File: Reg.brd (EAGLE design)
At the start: 15.2 x 21 mm, 12 parts, among them Q1 NPN2SC3422-2, Q2 NPN2SC3325, Q3 PNP2SA1313

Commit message: 完成
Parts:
- D1: value RED -> SHORT
- D2: value BLUE -> SHORT
- D3, D4: value (none) -> BLUE
- R1, R4: value 1k -> 1.5k
- R2: value DNP -> 1.5k
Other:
- board text added: "LED REG ver2"
- board text removed: "REG ver1"
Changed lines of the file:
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@@
 <setting verticaltext="up"/>
 </settings>
-<grid distance="12.5" unitdist="mil" unit="mil" style="lines" multiple="4" display="yes" altdistance="5" altunitdist="mil" altunit="mil"/>
+<grid distance="25" unitdist="mil" unit="mil" style="lines" multiple="4" display="yes" altdistance="5" altunitdist="mil" altunit="mil"/>
 <layers>
 <layer number="1" name="Top" color="4" fill="1" visible="yes" active="yes"/>
@@
 <board>
 <plain>
-<text x="3.81" y="18.0975" size="1.27" layer="21">REG ver1</text>
+<text x="14.2875" y="1.905" size="1.27" layer="21" rot="R90">LED REG ver2</text>
 <wire x1="0" y1="0" x2="15.24" y2="0" width="0.2032" layer="20"/>
 <wire x1="15.24" y1="0" x2="15.24" y2="20.955" width="0.2032" layer="20"/>
@@
 </autorouter>
 <elements>
-<element name="D1" library="my_rcl" package="D1608" value="RED" x="2.54" y="8.255" smashed="yes" rot="MR90">
+<element name="D1" library="my_rcl" package="D1608" value="SHORT" x="2.54" y="8.255" smashed="yes" rot="MR90">
 <attribute name="NAME" x="3.5075" y="7.455" size="0.8128" layer="26" rot="MR90"/>
 <attribute name="VALUE" x="0.89" y="7.455" size="0.8128" layer="28" rot="MR90"/>
 </element>
-<element name="D2" library="my_rcl" package="D1608" value="BLUE" x="2.54" y="4.7625" smashed="yes" rot="MR90">
-<attribute name="NAME" x="3.19" y="3.9625" size="0.8128" layer="26" rot="MR90"/>
+<element name="D2" library="my_rcl" package="D1608" value="SHORT" x="2.54" y="4.7625" smashed="yes" rot="MR90">
+<attribute name="NAME" x="3.825" y="3.9625" size="0.8128" layer="26" rot="MR90"/>
 <attribute name="VALUE" x="0.89" y="3.9625" size="0.8128" layer="28" rot="MR90"/>
 </element>
 <element name="JP1" library="pinhead" library_urn="urn:adsk.eagle:library:325" package="1X03" package3d_urn="urn:adsk.eagle:package:22458/2" value="CON" x="7.62" y="2.54" smashed="yes">
 <attribute name="POPULARITY" value="92" x="25.4" y="-1.27" size="1.778" layer="27" display="off"/>
-<attribute name="VALUE" x="3.81" y="-0.635" size="1.27" layer="27"/>
 </element>
 <element name="Q1" library="my_ic" package="TO126-2" value="NPN2SC3422-2" x="7.62" y="6.6675" smashed="yes">
-<attribute name="NAME" x="9.525" y="4.445" size="0.8128" layer="25"/>
+<attribute name="NAME" x="13.335" y="15.24" size="0.8128" layer="25" rot="R90"/>
 <attribute name="VALUE" x="3.81" y="9.8425" size="0.8128" layer="27"/>
 </element>
 <element name="Q2" library="my_ic" package="SC59" value="NPN2SC3325" x="9.2075" y="10.16" smashed="yes" rot="MR180">
-<attribute name="NAME" x="7.3025" y="10.795" size="0.8128" layer="26" rot="MR270"/>
+<attribute name="NAME" x="10.16" y="13.0175" size="0.8128" layer="26" rot="MR180"/>
 <attribute name="VALUE" x="7.3025" y="13.335" size="0.8128" layer="28" rot="MR180"/>
 </element>
-<element name="R2" library="my_rcl" package="1608" value="DNP" x="12.7" y="4.7625" smashed="yes" rot="MR90">
-<attribute name="NAME" x="12.395" y="8.3025" size="0.8128" layer="26" rot="MR0"/>
+<element name="R2" library="my_rcl" package="1608" value="1.5k" x="12.7" y="4.7625" smashed="yes" rot="MR90">
+<attribute name="NAME" x="14.5575" y="5.41" size="0.8128" layer="26" rot="MR270"/>
 <attribute name="VALUE" x="10.9" y="3.1625" size="0.8128" layer="28" rot="MR90"/>
 </element>
 <element name="Q3" library="my_ic" package="SC59" value="PNP2SA1313" x="5.08" y="10.16" smashed="yes" rot="MR180">
-<attribute name="NAME" x="4.445" y="7.9375" size="0.8128" layer="26" rot="MR180"/>
+<attribute name="NAME" x="3.4925" y="12.7" size="0.8128" layer="26" rot="MR270"/>
 <attribute name="VALUE" x="3.175" y="13.335" size="0.8128" layer="28" rot="MR180"/>
 </element>
-<element name="R1" library="my_rcl" package="1608" value="1k" x="2.54" y="10.795" smashed="yes" rot="R270">
-<attribute name="NAME" x="3.54" y="12.395" size="0.8128" layer="25" rot="R270"/>
+<element name="R1" library="my_rcl" package="1608" value="1.5k" x="2.54" y="10.795" smashed="yes" rot="R270">
+<attribute name="NAME" x="1.575" y="10.525" size="0.8128" layer="25" rot="R90"/>
 <attribute name="VALUE" x="0.74" y="12.395" size="0.8128" layer="27" rot="R270"/>
 </element>
-<element name="R4" library="my_rcl" package="1608" value="1k" x="2.54" y="7.62" smashed="yes" rot="R90">
-<attribute name="NAME" x="1.6" y="6.3025" size="0.8128" layer="25" rot="R180"/>
+<element name="R4" library="my_rcl" package="1608" value="1.5k" x="2.54" y="7.62" smashed="yes" rot="R90">
+<attribute name="NAME" x="0.6825" y="8.585" size="0.8128" layer="25" rot="R270"/>
 <attribute name="VALUE" x="4.34" y="6.02" size="0.8128" layer="27" rot="R90"/>
 </element>
 <element name="C7" library="my_rcl" package="1608" value="100p" x="7.3025" y="13.335" smashed="yes" rot="MR180">
-<attribute name="NAME" x="5.7025" y="12.335" size="0.8128" layer="26" rot="MR180"/>
+<attribute name="NAME" x="4.81" y="12.6875" size="0.8128" layer="26" rot="MR90"/>
 <attribute name="VALUE" x="5.7025" y="15.135" size="0.8128" layer="28" rot="MR180"/>
 </element>
-<element name="D3" library="my_rcl" package="D1608" value="" x="12.7" y="8.255" smashed="yes" rot="MR90">
+<element name="D3" library="my_rcl" package="D1608" value="BLUE" x="12.7" y="8.255" smashed="yes" rot="MR90">
 <attribute name="NAME" x="13.6675" y="7.455" size="0.8128" layer="26" rot="MR90"/>
 <attribute name="VALUE" x="11.05" y="7.455" size="0.8128" layer="28" rot="MR90"/>
 </element>
-<element name="D4" library="my_rcl" package="D1608" value="" x="12.7" y="11.43" smashed="yes" rot="MR90">
+<element name="D4" library="my_rcl" package="D1608" value="BLUE" x="12.7" y="11.43" smashed="yes" rot="MR90">
 <attribute name="NAME" x="13.6675" y="10.63" size="0.8128" layer="26" rot="MR90"/>
 <attribute name="VALUE" x="11.05" y="10.63" size="0.8128" layer="28" rot="MR90"/>

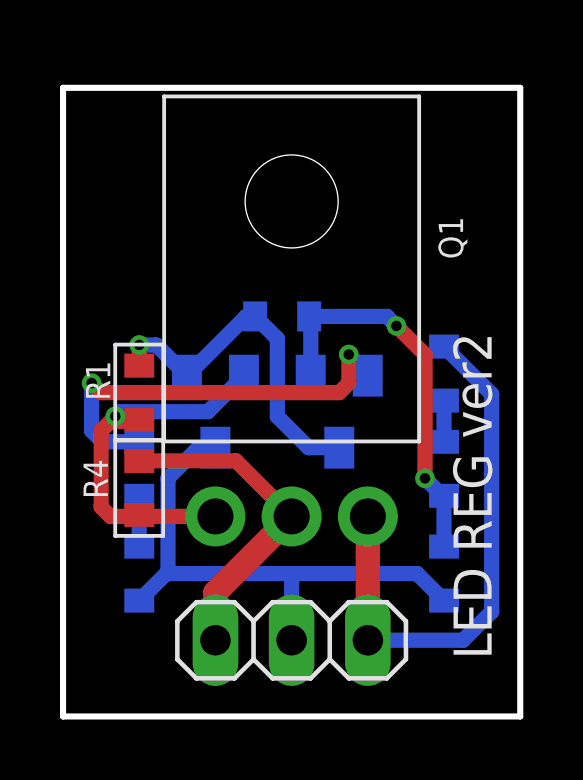
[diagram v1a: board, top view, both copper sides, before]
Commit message: 帰還ループの改善
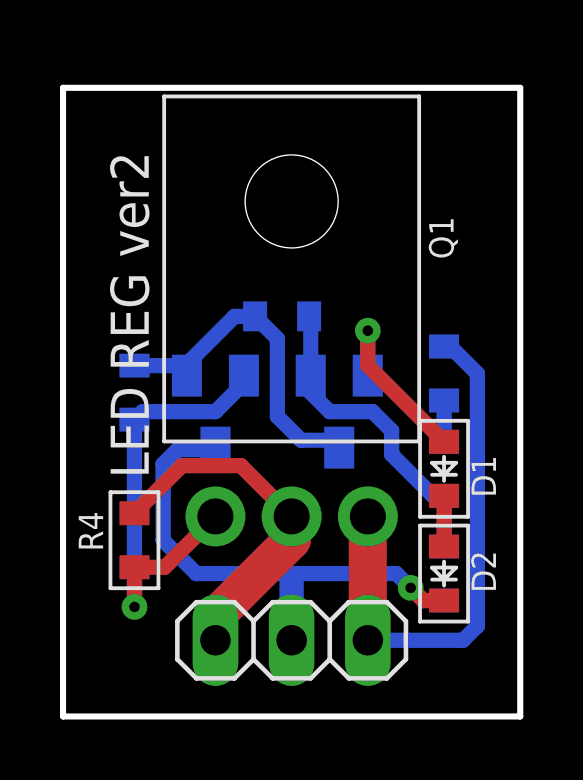
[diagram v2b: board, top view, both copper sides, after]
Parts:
- moved D1 10.2 mm to (12.7, 8.26), flipped to the top
- moved D2 10.2 mm to (12.7, 4.76), flipped to the top
- moved R4 1.75 mm to (2.38, 5.87)
- moved R1 0.16 mm to (2.38, 10.8), flipped to the bottom
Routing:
- net N$4: track 14.1 -> 6.26 mm, vias 2 -> 1
- net N$3: track 13.1 -> 10.6 mm, vias 2 -> 0
- net N$1: track 13.0 -> 15.4 mm
- net IN: track 11.0 -> 11.8 mm
- net N$10: track 11.9 -> 11.3 mm, vias 1 -> 0
- net GND: track 18.3 -> 18.2 mm, vias 0 -> 1

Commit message: チップオンリーも
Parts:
- added Q4: NPN2SC3325, my_ic:SC59
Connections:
- net IN: now also Q4.3
- net N$1: now also Q4.1
- net OUT: now also Q4.2
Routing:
- net OUT: track 17.9 -> 24.3 mm
- net N$1: track 15.4 -> 19.6 mm, vias 1 -> 2
- net IN: track 11.8 -> 14.2 mm
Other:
- board size 15.2 x 21 mm -> 25.4 x 21 mm
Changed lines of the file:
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@@
 <setting verticaltext="up"/>
 </settings>
-<grid distance="6.25" unitdist="mil" unit="mil" style="lines" multiple="4" display="yes" altdistance="5" altunitdist="mil" altunit="mil"/>
+<grid distance="12.5" unitdist="mil" unit="mil" style="lines" multiple="4" display="yes" altdistance="5" altunitdist="mil" altunit="mil"/>
 <layers>
 <layer number="1" name="Top" color="4" fill="1" visible="yes" active="yes"/>
@@
 <wire x1="15.24" y1="20.955" x2="0" y2="20.955" width="0.2032" layer="20"/>
 <wire x1="0" y1="20.955" x2="0" y2="0" width="0.2032" layer="20"/>
+<wire x1="15.24" y1="20.955" x2="25.4" y2="20.955" width="0.2032" layer="20"/>
+<wire x1="25.4" y1="20.955" x2="25.4" y2="0" width="0.2032" layer="20"/>
+<wire x1="25.4" y1="0" x2="15.24" y2="0" width="0.2032" layer="20"/>
 </plain>
 <attributes>
@@
 <attribute name="VALUE" x="11.05" y="10.63" size="0.8128" layer="28" rot="MR90"/>
 </element>
+<element name="Q4" library="my_ic" package="SC59" value="NPN2SC3325" x="6.35" y="10.795" smashed="yes" rot="R90">
+<attribute name="NAME" x="4.1275" y="8.89" size="0.8128" layer="25" rot="R90"/>
+<attribute name="VALUE" x="9.525" y="8.89" size="0.8128" layer="27" rot="R90"/>
+</element>
 </elements>
 <signals>
@@
 <wire x1="13.335" y1="2.54" x2="10.16" y2="2.54" width="0.508" layer="16"/>
 <wire x1="13.81125" y1="11.43" x2="13.81125" y2="3.01625" width="0.508" layer="16"/>
+<contactref element="Q4" pad="2"/>
+<wire x1="7.55" y1="11.745" x2="7.94" y2="11.745" width="0.8128" layer="1"/>
+<wire x1="10.16" y1="9.525" x2="10.16" y2="6.6675" width="0.8128" layer="1"/>
+<wire x1="7.94" y1="11.745" x2="10.16" y2="9.525" width="0.8128" layer="1"/>
 </signal>
 <signal name="IN">
@@
 <wire x1="5.08" y1="3.33375" x2="5.08" y2="2.54" width="1.27" layer="1"/>
 <wire x1="7.62" y1="5.87375" x2="5.08" y2="3.33375" width="1.27" layer="1"/>
-<wire x1="5.92625" y1="8.36125" x2="3.96875" y2="8.36125" width="0.508" layer="1"/>
-<wire x1="2.38125" y1="6.77375" x2="3.96875" y2="8.36125" width="0.508" layer="1"/>
-<wire x1="5.92625" y1="8.36125" x2="7.62" y2="6.6675" width="0.508" layer="1"/>
+<wire x1="3.96875" y1="8.36125" x2="2.38125" y2="6.77375" width="0.508" layer="1"/>
+<contactref element="Q4" pad="3"/>
+<wire x1="5.15" y1="10.795" x2="5.15" y2="8.5025" width="0.8128" layer="1"/>
+<wire x1="5.785" y1="8.5025" x2="5.15" y2="8.5025" width="0.8128" layer="1"/>
+<wire x1="7.62" y1="6.6675" x2="5.785" y2="8.5025" width="0.8128" layer="1"/>
+<wire x1="5.15" y1="8.5025" x2="5.00875" y2="8.36125" width="0.508" layer="1"/>
+<wire x1="5.00875" y1="8.36125" x2="3.96875" y2="8.36125" width="0.508" layer="1"/>
 </signal>
 <signal name="N$2">
@@
 <via x="2.38125" y="3.65125" extent="1-16" drill="0.35"/>
 <wire x1="2.38125" y1="3.65125" x2="2.38125" y2="4.97375" width="0.508" layer="1"/>
+<contactref element="Q4" pad="1"/>
+<wire x1="7.55" y1="9.845" x2="7.55" y2="9.455" width="0.508" layer="1"/>
+<wire x1="7.55" y1="9.455" x2="6.985" y2="8.89" width="0.508" layer="1"/>
+<via x="6.985" y="8.89" extent="1-16" drill="0.35"/>
+<wire x1="6.985" y1="8.89" x2="5.08" y2="6.985" width="0.508" layer="16"/>
+<wire x1="5.08" y1="6.985" x2="5.08" y2="6.6675" width="0.508" layer="16"/>
 </signal>
 <signal name="N$10">
@@
 <contactref element="C7" pad="1"/>
 <wire x1="9.2075" y1="8.96" x2="8.96" y2="9.2075" width="0.508" layer="16"/>
-<wire x1="8.96" y1="9.2075" x2="7.9375" y2="9.2075" width="0.508" layer="16"/>
-<wire x1="7.9375" y1="9.2075" x2="7.14375" y2="10.00125" width="0.508" layer="16"/>
+<wire x1="8.96" y1="9.2075" x2="8.255" y2="9.2075" width="0.508" layer="16"/>
+<wire x1="8.255" y1="9.2075" x2="7.14375" y2="10.31875" width="0.508" layer="16"/>
 <wire x1="7.14375" y1="12.59375" x2="6.4025" y2="13.335" width="0.508" layer="16"/>
-<wire x1="7.14375" y1="10.00125" x2="7.14375" y2="12.59375" width="0.508" layer="16"/>
+<wire x1="7.14375" y1="10.31875" x2="7.14375" y2="12.59375" width="0.508" layer="16"/>
 <wire x1="6.4025" y1="13.335" x2="5.715" y2="13.335" width="0.508" layer="16"/>
 <wire x1="4.13" y1="11.75" x2="4.13" y2="11.36" width="0.508" layer="16"/>

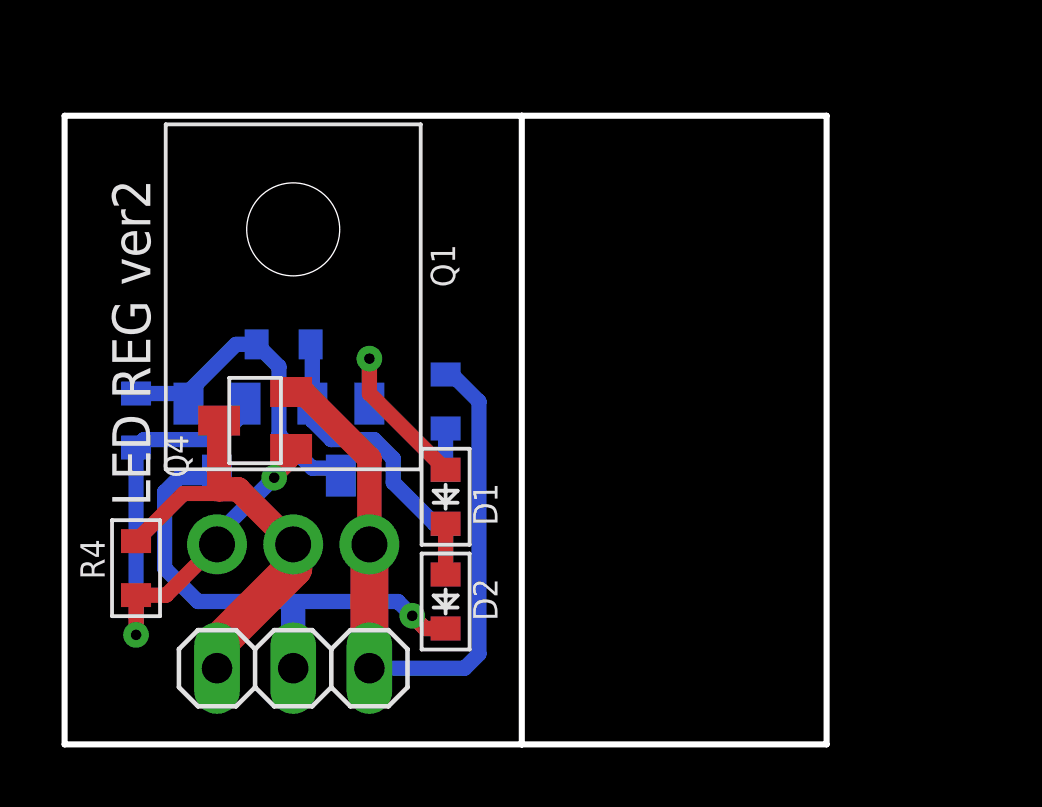
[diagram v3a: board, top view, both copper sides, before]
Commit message: ダーリントン、二段増幅を追加
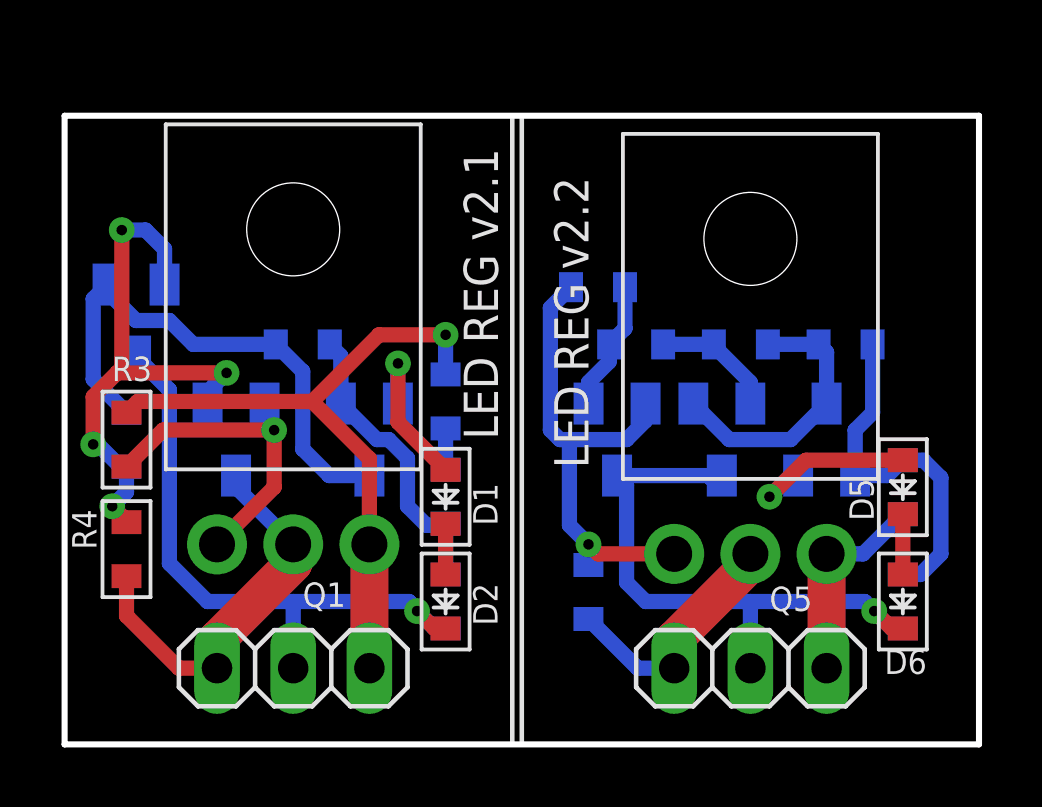
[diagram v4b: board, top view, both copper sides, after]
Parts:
- added C1: 100p, my_rcl:1608
- added D5, D6: BLUE, my_rcl:D1608
- added JP2: CON, pinhead:1X03
- added Q5: NPN2SC3422-2, my_ic:TO126-2
- added Q6: NPN2SC3325, my_ic:SC59
- added Q7, Q8: PNP2SA1313, my_ic:SC59
- added R10: 0.75k, my_rcl:1608
- added R12, R5, R6, R7, R9: 1.5k, my_rcl:1608
- added R3: 10k, my_rcl:1608
- moved Q3 4.80 mm to (2.38, 14.1)
- moved Q2 0.95 mm to (10.2, 10.2)
- moved Q4 0.90 mm to (5.71, 10.2), flipped to the bottom, turned to 180 degrees
- moved R1 0.71 mm to (2.06, 10.2)
- moved R4 0.71 mm to (2.06, 6.51), turned to 270 degrees
- moved C7 0.63 mm to (7.94, 13.3)
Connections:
- new net GND1: D6.K, JP2.2, Q7.3, Q8.3, R5.1
- new net IN1: JP2.1, Q5.2, R9.2
- new net N$11: Q7.2, R6.2, R7.1
- new net N$12: C1.1, Q6.3, Q7.1, R6.1
- new net N$13: C1.2, Q6.1, R12.1, R5.2
- new net N$15: Q8.1, R10.1, R7.2
- new net N$16: Q5.3, Q8.2, R10.2, R9.1
- new net N$6: Q1.3, Q4.2, R3.2
- new net N$8: D5.K, D6.A
- new net N$9: D5.A, Q6.2
- new net OUT1: JP2.3, Q5.1, R12.2
- net N$1: no longer Q1.3
- net OUT: now also R3.1; no longer Q4.2
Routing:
- net GND1: track 0.00 -> 20.6 mm, vias 0 -> 1
- net N$16: track 0.00 -> 16.6 mm, vias 0 -> 1
- net N$13: track 0.00 -> 12.0 mm
- net N$6: track 0.00 -> 11.0 mm, vias 0 -> 1
- net N$12: track 0.00 -> 9.21 mm
- net IN1: track 0.00 -> 8.40 mm
- net OUT1: track 0.00 -> 6.90 mm
- net N$10: track 11.2 -> 18.0 mm
- net N$9: track 0.00 -> 6.20 mm, vias 0 -> 1
- net N$15: track 0.00 -> 4.38 mm
- net N$11: track 0.00 -> 4.17 mm
- net GND: track 18.2 -> 20.9 mm
- net N$8: track 0.00 -> 2.01 mm
- net OUT: track 24.3 -> 22.7 mm, vias 0 -> 1
- net IN: track 14.2 -> 13.3 mm
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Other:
- board size 25.4 x 21 mm -> 30.5 x 21 mm
- board text added: "LED REG v2.1"
- board text added: "LED REG v2.2"
- board text removed: "LED REG ver2"
